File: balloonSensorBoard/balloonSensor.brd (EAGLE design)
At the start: 90.2 x 53.3 mm, 29 parts, among them U1 ARDUINO-MEGAPRO

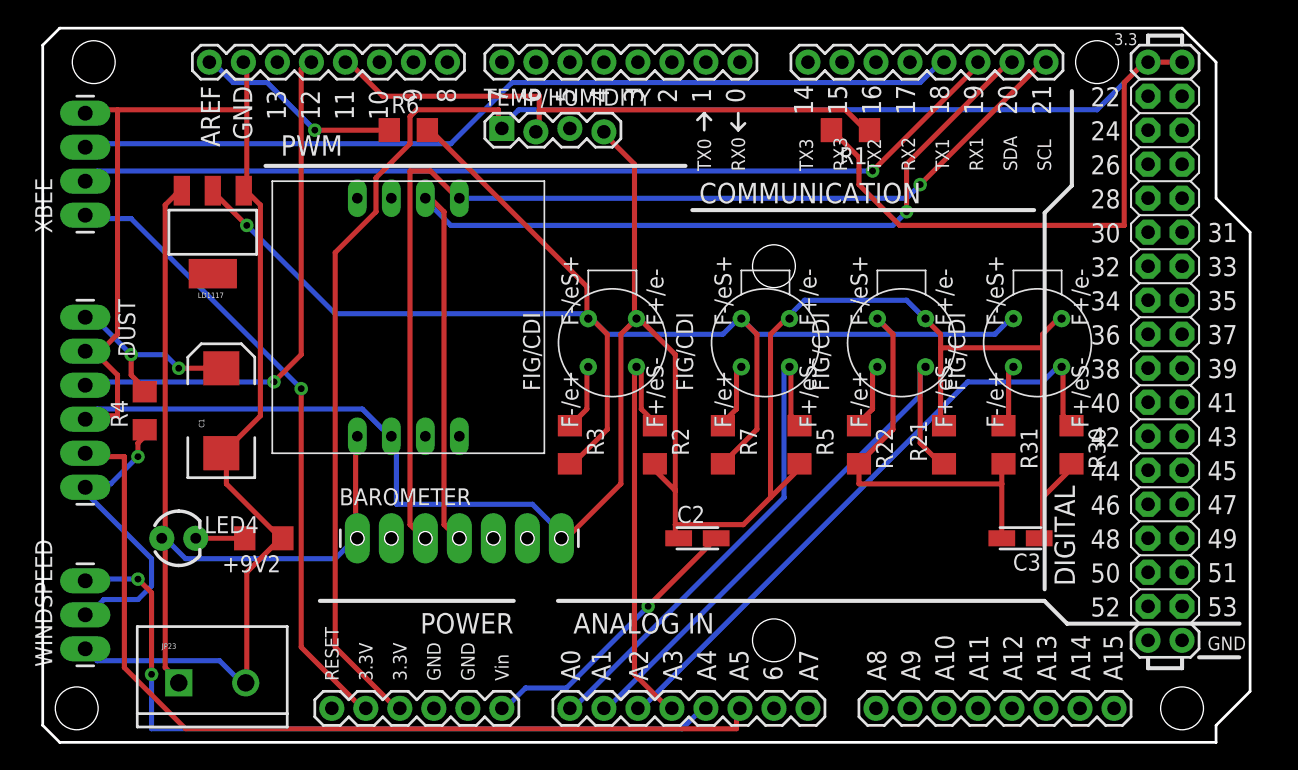
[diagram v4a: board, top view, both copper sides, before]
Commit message: added top copper text
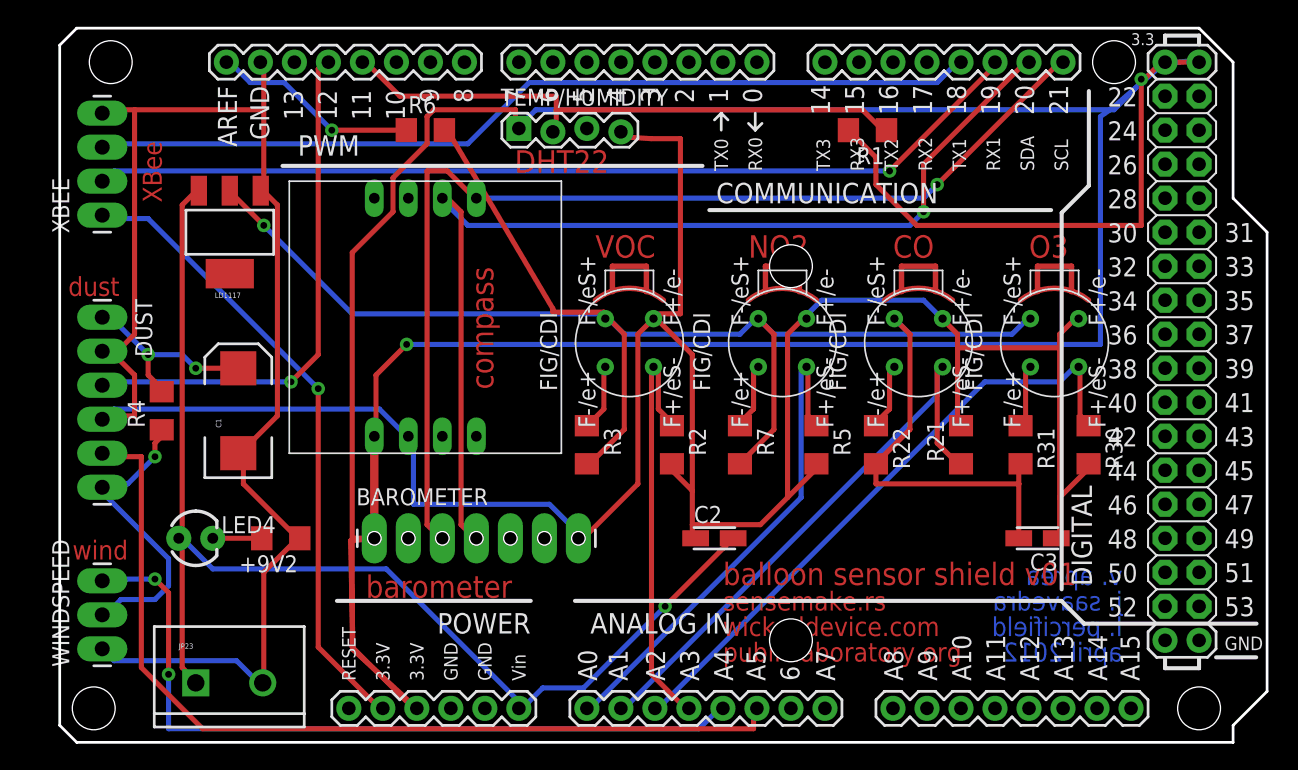
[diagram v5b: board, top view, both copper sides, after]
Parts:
- moved R30 1.27 mm to (78.1, 22.2)
- moved R31 1.27 mm to (73.0, 22.2)
- moved R2 1.27 mm to (47.0, 22.2)
- moved R3 1.27 mm to (40.6, 22.2)
- moved R7 1.27 mm to (52.1, 22.2)
- moved TEMP/HUMIDITY 1.27 mm to (35.6, 45.7)
- moved LD1117 1.27 mm to (14.0, 38.1)
- moved DUST 1.27 mm to (4.45, 31.8)
- moved R4 1.27 mm to (8.89, 24.8)
- moved WINDSPEED 1.27 mm to (4.45, 6.99)
- moved XBEE 1.27 mm to (4.45, 39.4)
- moved U1 1.27 mm to (1.27, 0.00)
- moved +9V2 1.27 mm to (17.8, 15.2)
- moved BAROMETER 1.27 mm to (24.8, 15.2)
- moved C1 1.27 mm to (14.6, 24.8)
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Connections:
- net 5V: no longer U1.5V@0, U1.5V@1, U1.5V@2
- net VCC: now also U1.5V@0, U1.5V@1, U1.5V@2
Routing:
- net VCC: track 7.75 -> 121.7 mm, vias 0 -> 1
- net N$6: track 0.00 -> 25.4 mm
- net N$3: track 0.00 -> 20.3 mm
- net +9V: track 75.3 -> 90.3 mm
- net GND: track 277.2 -> 282.6 mm
- net 5V: track 148.9 -> 146.0 mm, vias 0 -> 1
- net V+: track 141.9 -> 143.0 mm
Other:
- board text added: "CO"
- board text added: "DHT22"
- board text added: "NO2"
- board text added: "O3"
- board text added: "VOC"
- board text added: "XBee"
- board text added: "april 2012"
- board text added: "balloon sensor shield v01"
- board text added: "barometer"
- board text added: "compass"
- board text added: "dust"
- board text added: "j. saavedra"
- board text added: "l. percifield"
- board text added: "publiclaboratory.org"
- board text added: "sensemake.rs"
- board text added: "v. aprea"
- board text added: "wickeddevice.com"
- board text added: "wind"

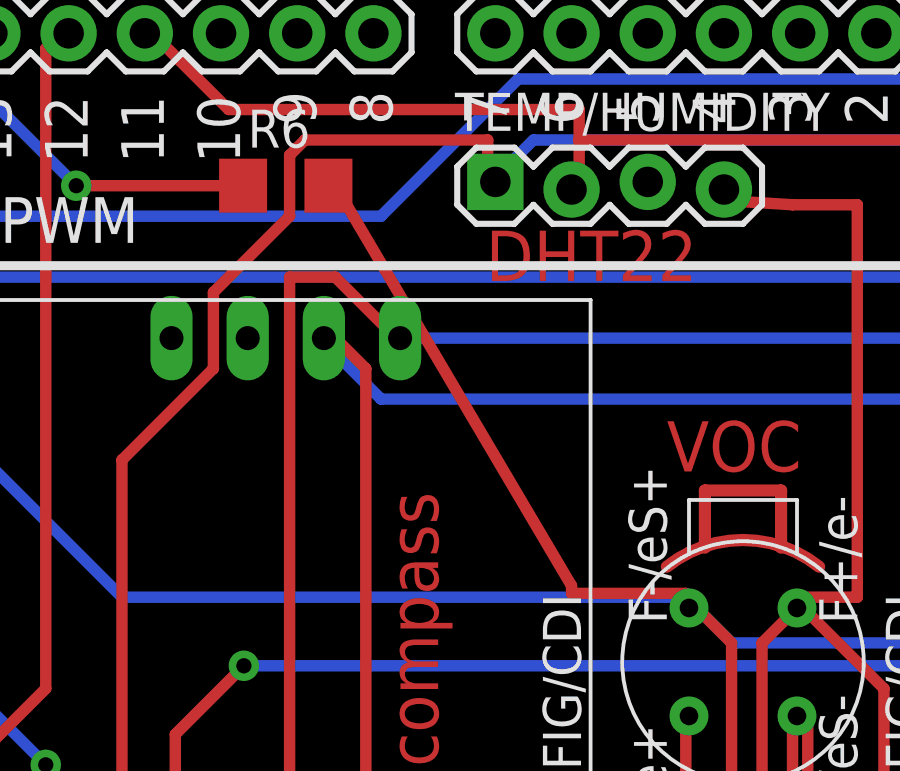
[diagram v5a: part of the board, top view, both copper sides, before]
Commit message: fixed shorted trace near compass pin 5
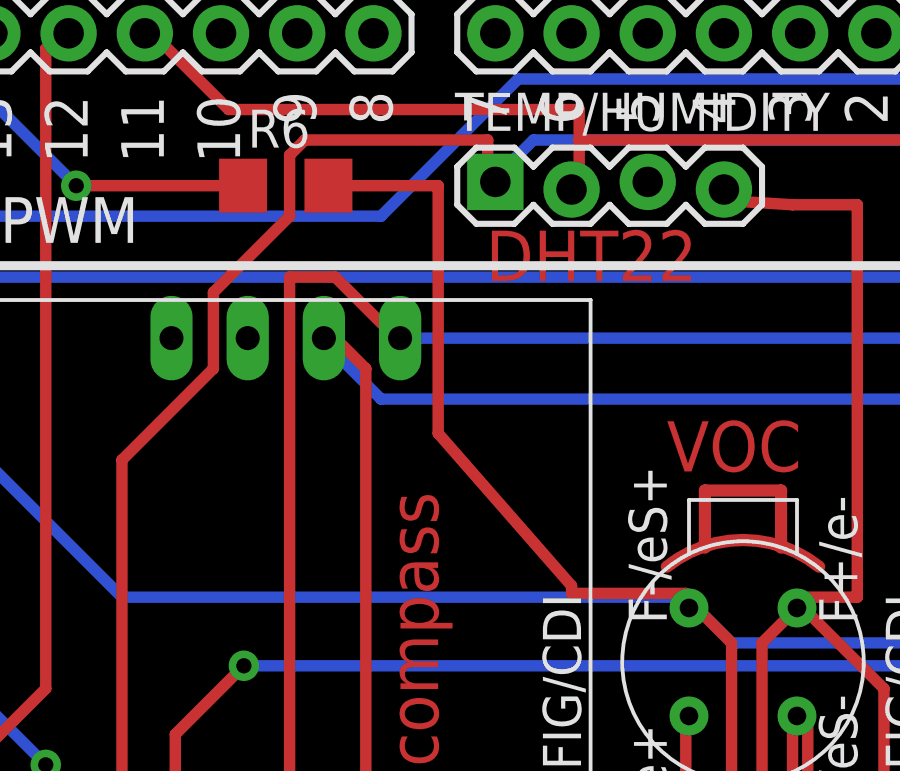
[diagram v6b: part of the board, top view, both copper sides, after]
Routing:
- net V+: track 143.0 -> 145.9 mm
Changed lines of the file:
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@@
 <wire x1="41.91" y1="32.131" x2="38.1" y2="32.131" width="0.381" layer="1"/>
 <wire x1="38.1" y1="32.131" x2="38.1" y2="32.385" width="0.381" layer="1"/>
-<wire x1="38.1" y1="32.385" x2="30.226" y2="45.72" width="0.381" layer="1"/>
+<wire x1="38.1" y1="32.385" x2="33.655" y2="37.465" width="0.381" layer="1"/>
+<wire x1="33.655" y1="37.465" x2="33.655" y2="45.72" width="0.381" layer="1"/>
+<wire x1="33.655" y1="45.72" x2="29.997" y2="45.72" width="0.381" layer="1"/>
 <wire x1="41.91" y1="32.004" x2="41.91" y2="32.131" width="0.381" layer="1"/>
-<wire x1="30.226" y1="45.72" x2="29.997" y2="45.72" width="0.381" layer="1"/>
 <wire x1="41.91" y1="32.004" x2="42.015" y2="31.645" width="0.381" layer="1"/>
 <wire x1="16.51" y1="38.608" x2="13.97" y2="41.148" width="0.381" layer="1"/>

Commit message: updated resistors
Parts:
- R31: value 60 ohm -> 80 ohm
- R7: value 34 ohm -> 120 ohm
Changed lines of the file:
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@@
 <element name="NO2" library="ricardo" package="SR-4" value="E2V NO2" x="55.245" y="29.845" rot="R90"/>
 <element name="R5" library="rcl" package="R1206" value="220k" x="57.785" y="22.225" rot="R270"/>
-<element name="R7" library="rcl" package="R1206" value="34 ohm" x="52.07" y="22.225" rot="R270"/>
+<element name="R7" library="rcl" package="R1206" value="120 ohm" x="52.07" y="22.225" rot="R270"/>
 <element name="O3" library="ricardo" package="SR-4" value="E2V Ozone" x="75.565" y="29.845" rot="R90"/>
 <element name="R30" library="rcl" package="R1206" value="220k" x="78.105" y="22.225" rot="R270"/>
-<element name="R31" library="rcl" package="R1206" value="60 ohm" x="73.025" y="22.225" rot="R270"/>
+<element name="R31" library="rcl" package="R1206" value="80 ohm" x="73.025" y="22.225" rot="R270"/>
 <element name="JP23" library="SparkFun" package="SCREWTERMINAL-5MM-2" value="Screw Terminal" x="11.43" y="4.445"/>
 <element name="R1" library="rcl" package="R1206" value="10k" x="61.595" y="45.72" rot="R180"/>
